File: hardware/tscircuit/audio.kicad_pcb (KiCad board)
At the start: 2 copper layers, 80 x 60 mm, 22 parts

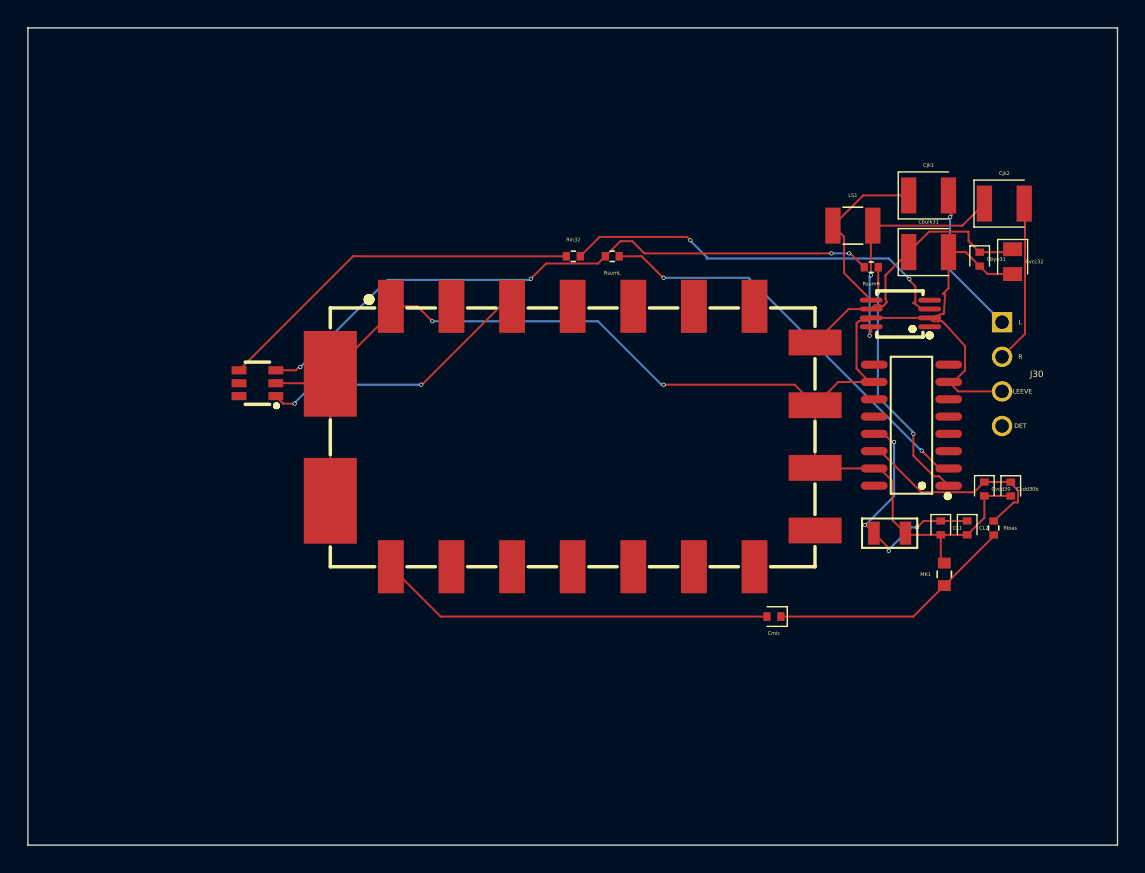
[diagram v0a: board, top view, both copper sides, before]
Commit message: hw: fix 6 issues from realized-board self-review (2 blockers)
Adversarial multi-agent review of the real-parts board caught 6 real defects the
per-sheet DRC couldn't see; all datasheet-verified, fixed, sheets re-verified
(DRC parity=0 each):

- BLOCKER (power): BQ25887 SNS was tied to BAT externally -> shorts the internal
  charge-current shunt, defeating ICHG regulation on the 2S pack. SNS is now its own
  net (44uF to GND only); the SNS<->BAT shunt is internal.
- BLOCKER (expansion): PESD5V0S2UAT ESD arrays (common-cathode) had the common cathode
  on GND -> every I2C logic-high forward-biases the diode and clamps SDA/SCL to ~0.6V
  (whole bus dead). Cathode moved to +3V3 (clamps overshoot above the rail).
- MAJOR (audio): PAM8302 inputs were DC-coupled (IN- hard to GND) -> breaks the
  internal VDD/2 bias and rails the output. Added series 0.1uF caps on both inputs.
- MINOR (power): BQ25887 TS divider was missing RT2 (30.1k || NTC) -> shifted temp
  window; added.
- MINOR (power): MP2315 bootstraps were missing the datasheet-required 20R series
  resistor; added Rbst4/Rbst5.
- MINOR (rf): SP4T pins 1/8/11/12/14 are N/C per the SKY13414 datasheet -> untied from
  GND (only the EP paddle is ground).

GPIO45 (VDD_SPI strap on CC1101 GDO2) is handled by the set_flash_voltage eFuse (a
verifier false-positive) -> documented inline. Docs (power EN+RU) corrected.

Co-Authored-By: Claude Opus 4.8 <noreply@anthropic.com>
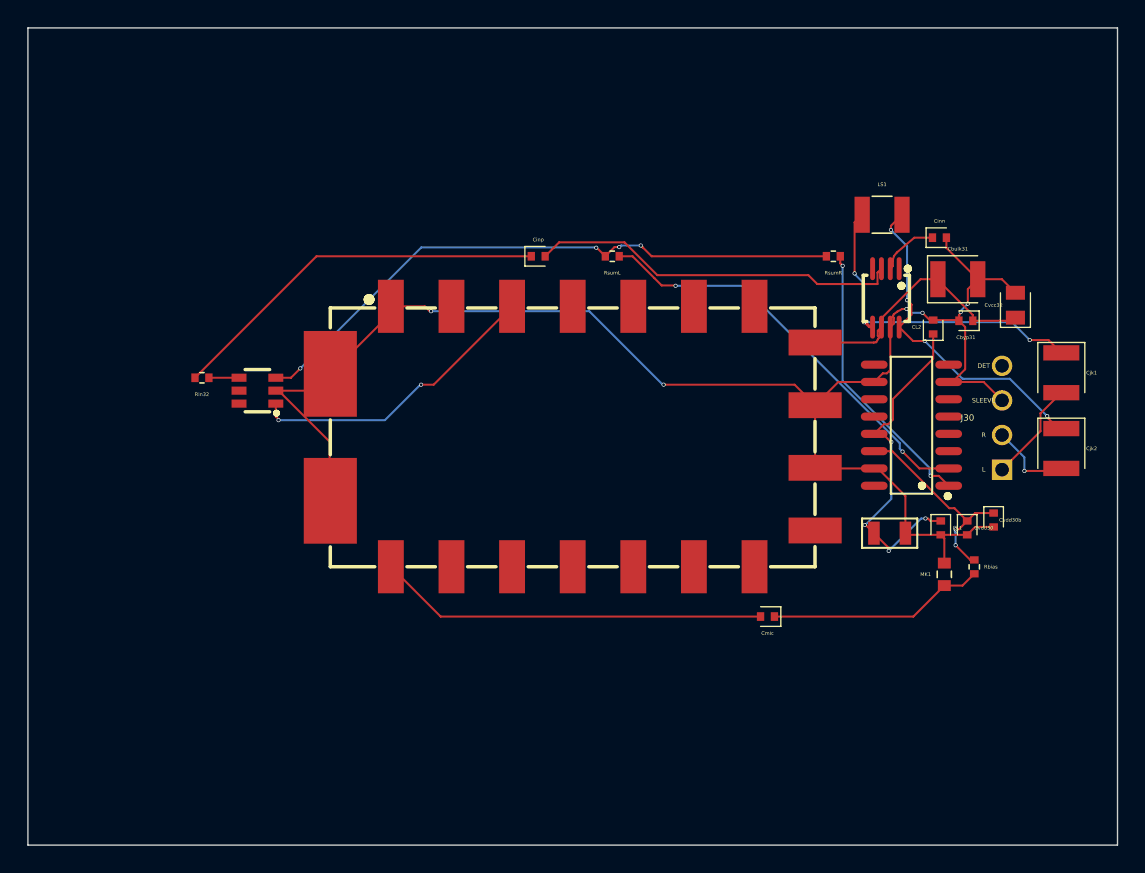
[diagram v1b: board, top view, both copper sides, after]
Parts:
- added Cinn: 0.1uF, tscircuit:capacitor_cap0402, F.Cu at (126.9, 85.4)
- added Cinp: 0.1uF, tscircuit:capacitor_cap0402, F.Cu at (97.5, 86.8)
- moved Rin32 28.7 mm to (72.8, 95.7), turned to 180 degrees
- moved Cjk2 18.5 mm to (135.9, 100.9), turned to -90 degrees
- moved Cjk1 16.3 mm to (135.9, 95.3), turned to -90 degrees
- moved CL2 15.0 mm to (126.5, 92.0), turned to 90 degrees
- moved Cbyp31 4.64 mm to (128.9, 91.5), turned to 180 degrees
- moved Cvcc32 3.21 mm to (132.5, 90.4), turned to 90 degrees
- moved J30 3.20 mm to (131.5, 98.6), turned to 90 degrees
- moved Rbias 3.19 mm to (129.5, 109.6)
- moved Cvdd30 3.13 mm to (129.0, 106.7)
- moved Cbulk31 2.93 mm to (128.3, 88.5)
- moved RsumR 2.90 mm to (119.1, 86.8)
- moved Cvdd30b 2.60 mm to (130.9, 106.1)
- moved LS1 2.29 mm to (122.7, 83.7)
- moved U32 1.56 mm to (123.0, 89.8), turned to 180 degrees
- moved U33 0.55 mm to (76.9, 96.6)
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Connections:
- Rin32 pad 2: .Rin32 > .pin2 to .U32 > .IN_POS -> .Rin32 > .pin2 to .Cinp > .pin1
- U32 pad 2: GND -> .U32 > .IN_NEG to .Cinn > .pin1
- U32 pad 3: .Rin32 > .pin2 to .U32 > .IN_POS -> .Cinp > .pin2 to .U32 > .IN_POS
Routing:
- net .Rin32 > .pin2 to .U32 > .IN_POS: track 29.5 -> 0.00 mm, vias 2 -> 0
- net .Rin32 > .pin2 to .Cinp > .pin1: track 0.00 -> 28.4 mm
- net .Cinp > .pin2 to .U32 > .IN_POS: track 0.00 -> 27.3 mm
- net MUX_OUT: track 27.5 -> 2.21 mm
- net SPK_P: track 13.1 -> 25.4 mm, vias 0 -> 4
- net .U30 > .RCLK to .Y1 > .OSC1: track 18.1 -> 25.3 mm
- net SPK_M: track 17.8 -> 24.6 mm, vias 2 -> 4
- net .Cjk2 > .pin2 to .J30 > .R: track 12.0 -> 6.11 mm, vias 0 -> 1
- net .U32 > .IN_NEG to .Cinn > .pin1: track 0.00 -> 4.52 mm
- net GND: track 119.6 -> 115.8 mm, vias 2 -> 6
- net .Cjk1 > .pin2 to .J30 > .L: track 11.0 -> 7.46 mm, vias 1 -> 0
- net SI_AUDIO: track 47.9 -> 45.3 mm
- net V3V3A: track 17.5 -> 15.3 mm, vias 0 -> 2
- net MIC_HOT: track 18.2 -> 16.0 mm
- net .U30 > .pin1 to .RsumR > .pin1: track 18.4 -> 20.5 mm
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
